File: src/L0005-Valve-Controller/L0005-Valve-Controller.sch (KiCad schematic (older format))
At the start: 14 parts, among them U1 LPC54113J256BD64QL

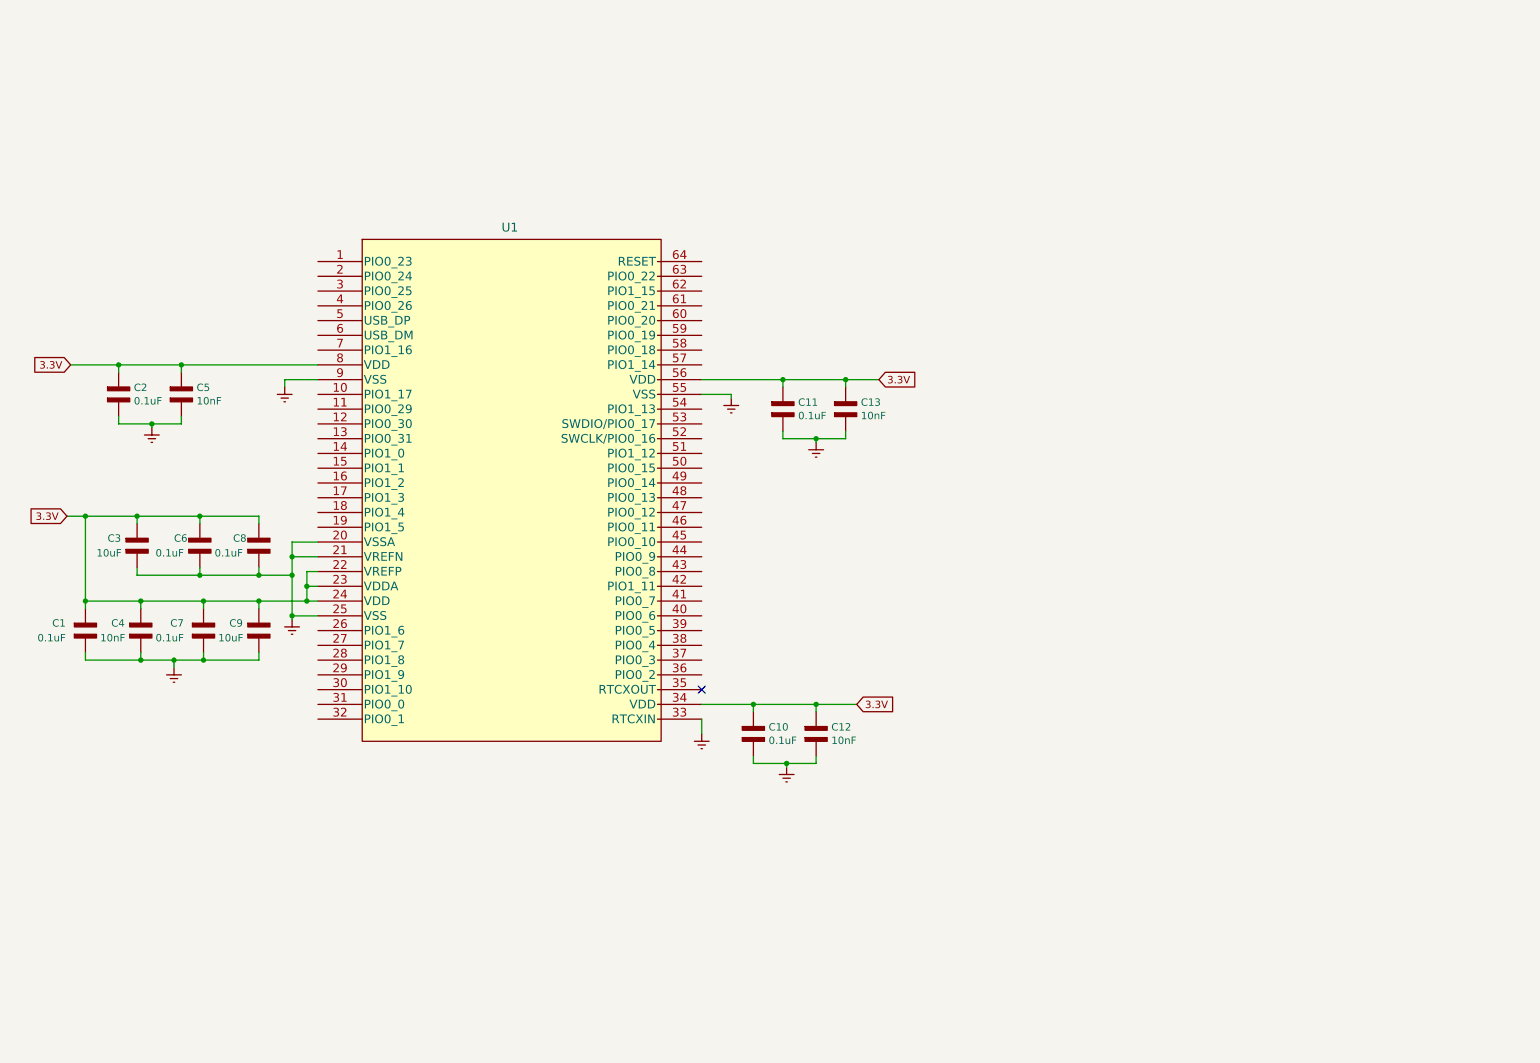
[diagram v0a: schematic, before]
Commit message: Added programmer to schematic
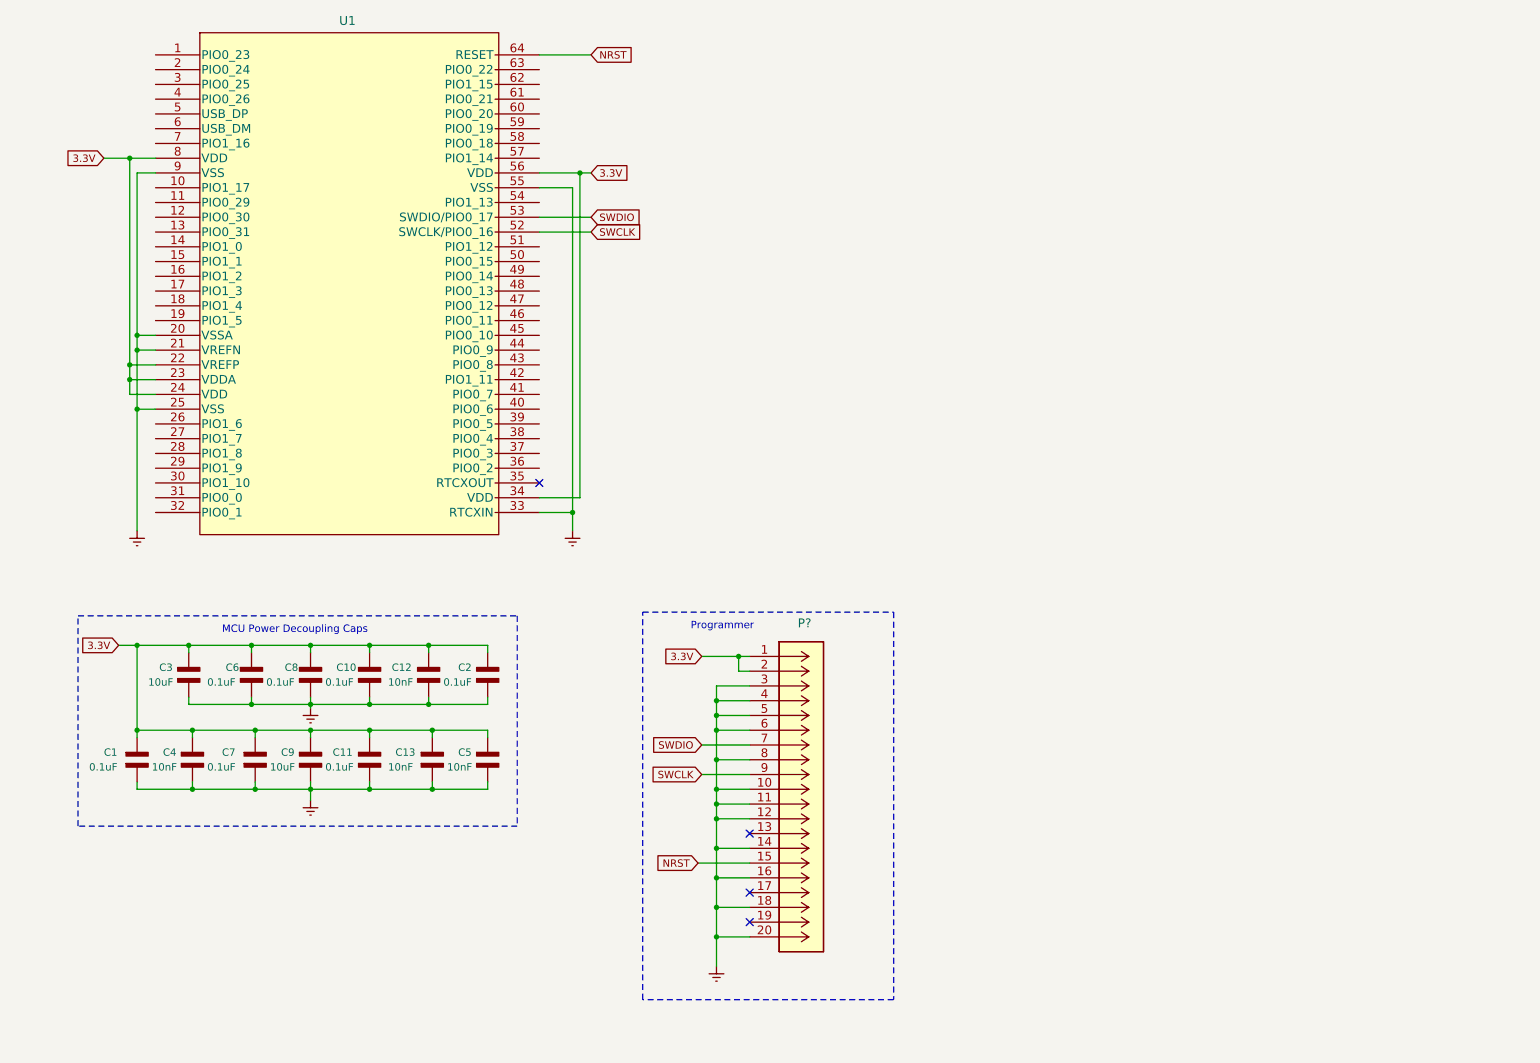
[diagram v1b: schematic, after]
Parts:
- added P?: 3220-20-0200-00, CONN20_D10-RA-BK_SUL, symbol L0005-Valve-Controller:3220-20-0200-00
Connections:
- net 3.3V: now also P?.1, P?.2
- net Earth: now also P?.10, P?.11, P?.12, P?.14, P?.16, P?.18, P?.20, P?.3, P?.4, P?.5, P?.6, P?.8
- net SWCLK: now reaches U1.52 (SWCLK/PIO0_16)
- net SWCLK: now also P?.9
- net SWDIO: now reaches U1.53 (SWDIO/PIO0_17)
- net SWDIO: now also P?.7
- net NRST: now reaches U1.64 (RESET)
- net NRST: now also P?.15
- no-connect marks 1 -> 4
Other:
- note added: "MCU Power Decoupling Caps"
- note added: "Programmer"
- moved on the sheet: C1, C10, C11, C12, C13, C2, C3, C4, C5, C6, C7, C8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

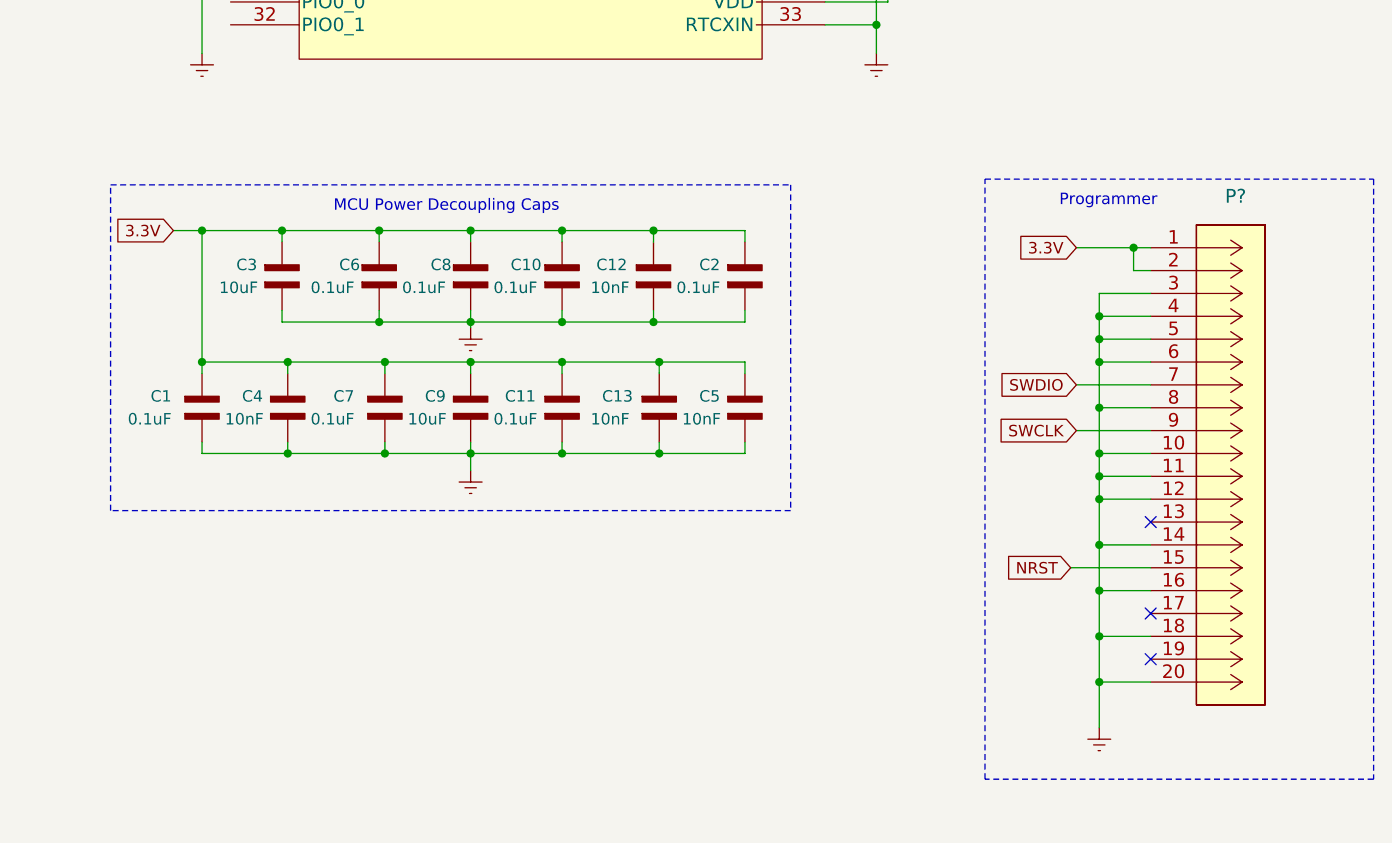
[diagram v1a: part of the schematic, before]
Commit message: Added power supply to schematic
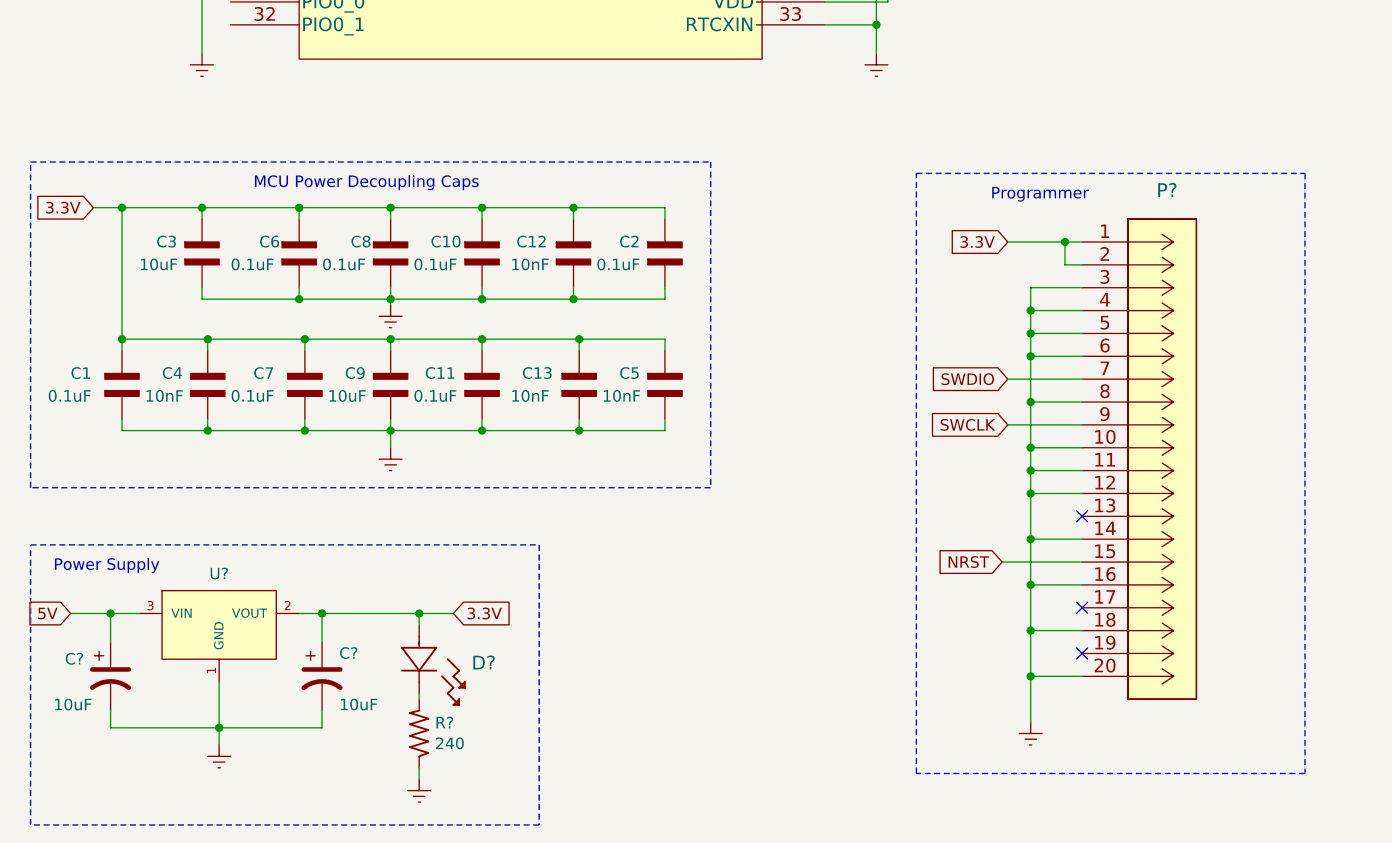
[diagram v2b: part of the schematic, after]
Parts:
- added C? (x2): 10uF, symbol L0005-Valve-Controller:CAP_Polar
- added D?: LED_GREEN, symbol L0005-Valve-Controller:LED_GREEN
- added R?: 240, symbol L0005-Valve-Controller:RES_0603
- added U?: LMS8117AMP-3.3_NOPB, symbol L0005-Valve-Controller:LMS8117AMP-3.3_NOPB
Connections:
- net 3.3V: now also C?.1, D?.2, U?.2 (VOUT)
- net Earth: now also C?.2, C?.2, R?.1, U?.1 (GND)
- new net: D?.1, R?.2
- new net 5V: C?.1, U?.3 (VIN)
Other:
- note added: "Power Supply"
- moved on the sheet: C1, C10, C11, C12, C13, C2, C3, C4, C5, C6, C7, C8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

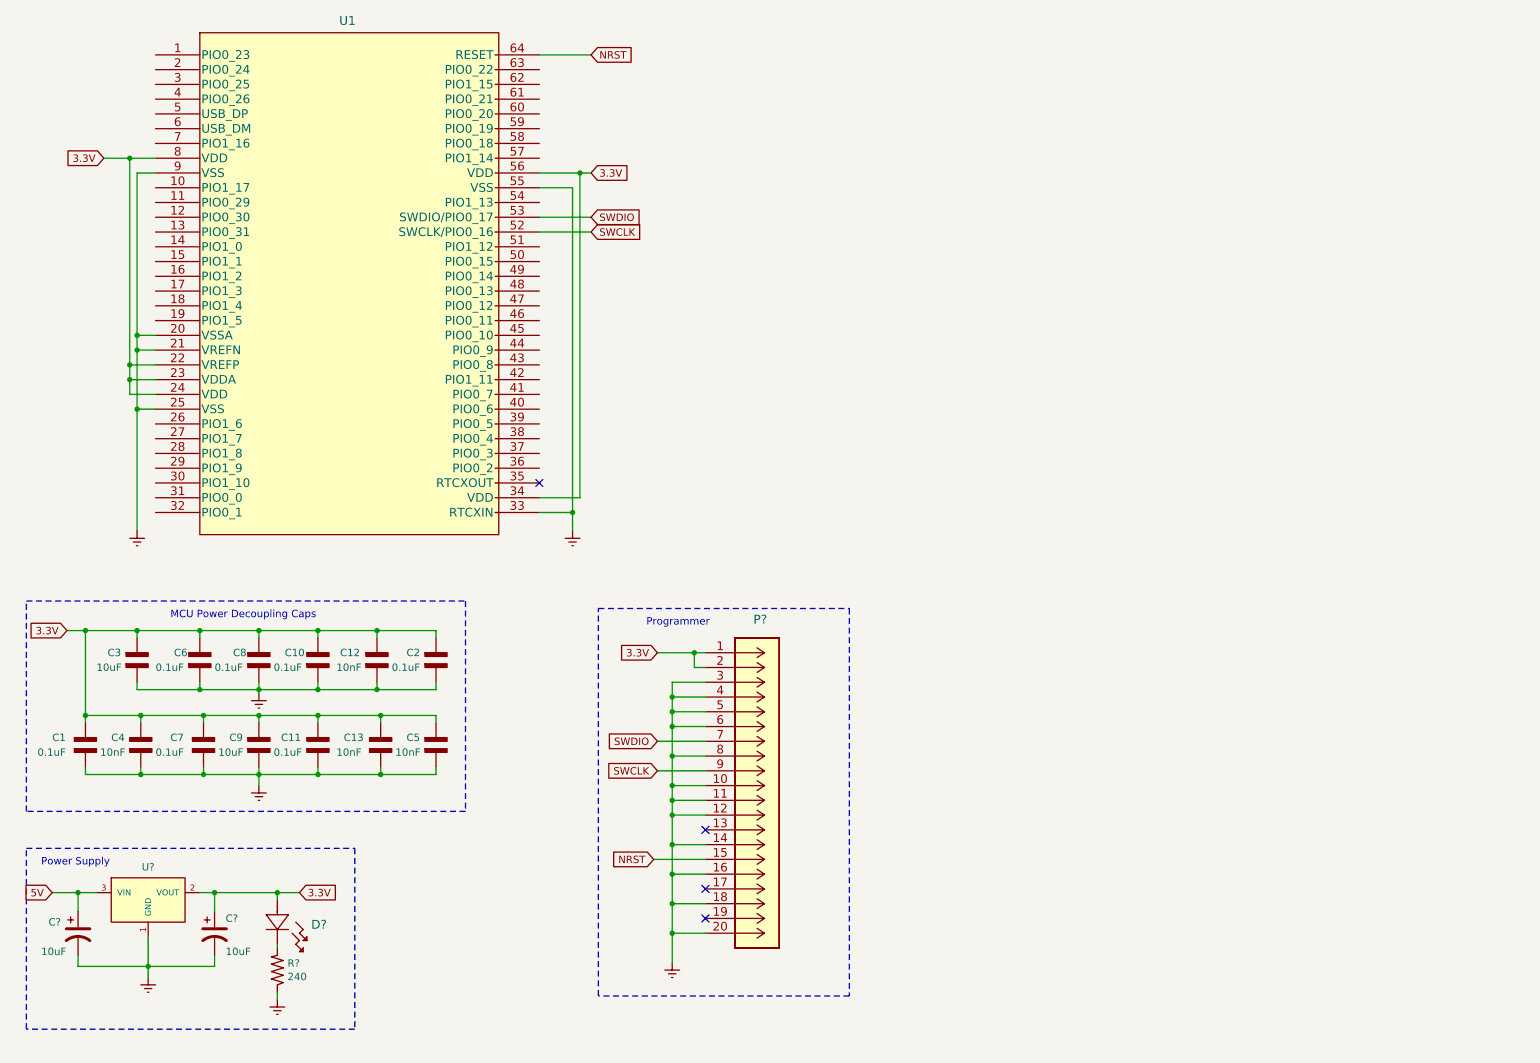
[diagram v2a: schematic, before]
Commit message: Added UART interface to schematic
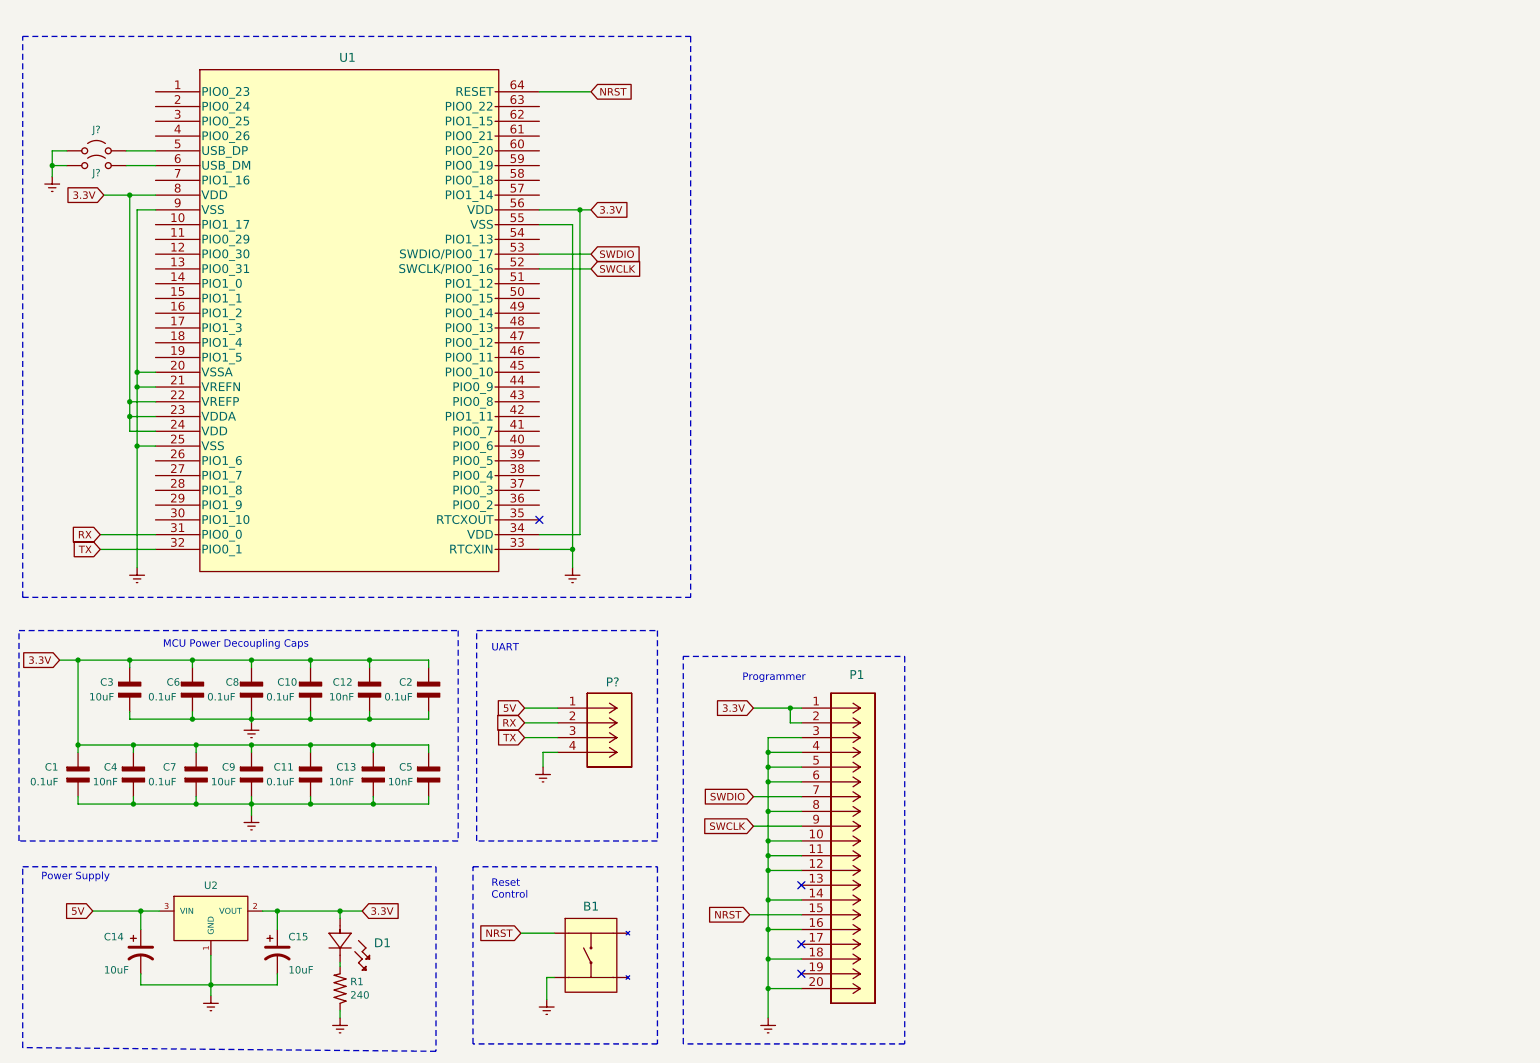
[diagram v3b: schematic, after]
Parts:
- added B1: PTS647SM38SMTR2LFS, SW_PTS647SM38SMTR2LFS_CNK, symbol L0005-Valve-Controller:PTS647SM38SMTR2LFS
- added J? (x2): Jumper_NO, symbol L0005-Valve-Controller:Jumper_NO
- added P?: 140-504-415-000, CONN_4840.2201_SCH, symbol L0005-Valve-Controller:140-504-415-000
- gave numbers to parts that had none: 6
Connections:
- net 5V: now also P?.1 (+12V)
- net Earth: now also B1.3, J?.1 (A), J?.1 (A), P?.4
- net NRST: now also B1.1
- net RX: now reaches U1.31 (PIO0_0)
- net RX: now also P?.2 (GND)
- net TX: now reaches U1.32 (PIO0_1)
- net TX: now also P?.3
- net at U1.5 (USB_DP): now also J?.2 (B)
- net at U1.6 (USB_DM): now also J?.2 (B)
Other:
- note added: "Reset \nControl"
- note added: "UART"
- moved on the sheet: C1, C10, C11, C12, C13, C14, C15, C2, C3, C4, C5, C6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
